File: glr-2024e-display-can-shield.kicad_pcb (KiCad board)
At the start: 2 copper layers, 10 parts, among them CN12 Conn_02x08_Odd_Even, CN6 Conn_01x08, CN8 Conn_01x06, IC1 L9615D013TR, J1 Screw_Terminal_01x12

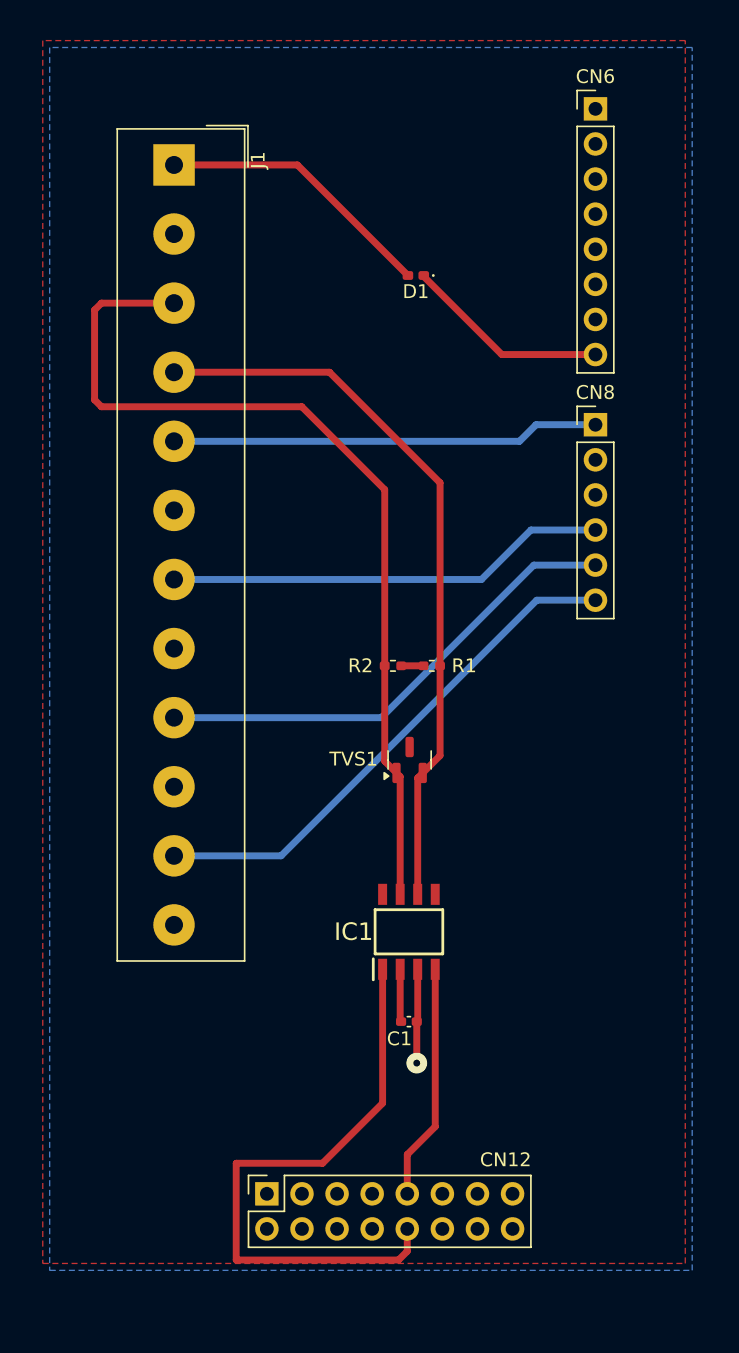
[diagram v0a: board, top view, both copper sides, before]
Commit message: make 4pin and 8pin screw terminal instead of 12pin
use exact footprint and 3d model

Co-Authored-By: wallalex0 <97884125+wallalex0@users.noreply.github.com>
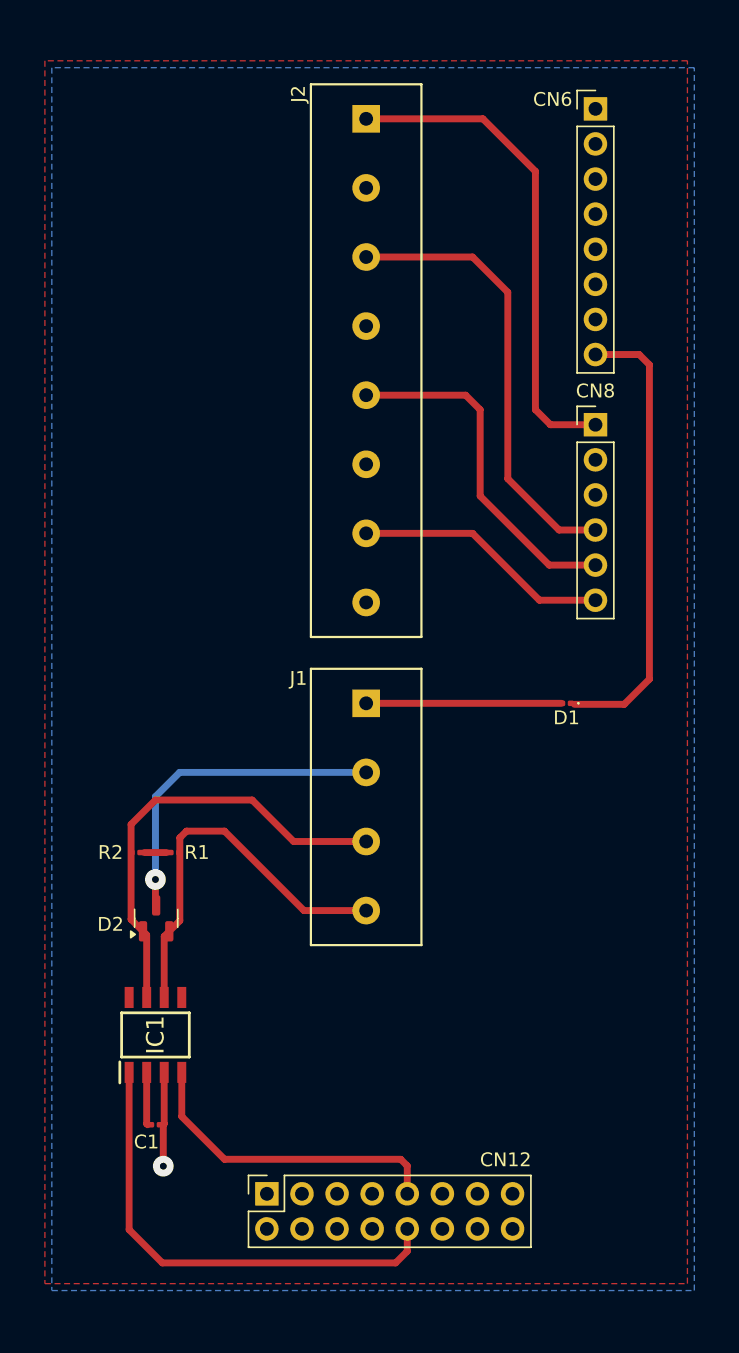
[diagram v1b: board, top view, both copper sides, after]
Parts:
- added J2: Screw_Terminal_01x08, GLR_KiCAD_Library:WECO-950-FB-08, F.Cu at (140.1, 47.7)
- C1: footprint Capacitor_SMD:C_0402_1005Metric_Pad0.74x0.62mm_HandSolder -> Capacitor_SMD:C_0201_0603Metric
- D1: footprint Diode_SMD:D_0402_1005Metric_Pad0.77x0.64mm_HandSolder -> Diode_SMD:D_0201_0603Metric
- J1: value Screw_Terminal_01x12 -> Screw_Terminal_01x04; footprint TerminalBlock_Altech:Altech_AK100_1x12_P5.00mm -> GLR_KiCAD_Library:WECO-950-FB-04
- R1, R2: footprint Resistor_SMD:R_0402_1005Metric_Pad0.72x0.64mm_HandSolder -> Resistor_SMD:R_0201_0603Metric
- moved J1 58.3 mm to (140.9, 110.0), turned to 180 degrees
- moved D1 32.8 mm to (155.0, 92.5)
- moved R1 23.0 mm to (126.7, 103.3)
- moved R2 23.0 mm to (123.8, 103.3)
- moved D2 21.6 mm to (125.3, 108.1)
- moved C1 19.8 mm to (125.2, 123.0)
- moved IC1 19.8 mm to (125.2, 116.5)
- renumbered TVS1 to D2
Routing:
- net /CAN H: track 65.9 -> 32.0 mm
- net /CAN L: track 53.0 -> 28.1 mm
- net GND: track 3.82 -> 27.7 mm, vias 0 -> 1
- net /button4: track 38.2 -> 18.6 mm
- net +6V to +9V: track 14.8 -> 33.1 mm
- net /button3: track 35.1 -> 25.4 mm
- net /Tx: track 43.3 -> 34.5 mm
- net Net-(D1-A): track 20.2 -> 14.1 mm
- net /Rx: track 17.1 -> 23.0 mm
- net /button1: track 31.0 -> 35.9 mm
- net /button2: track 32.0 -> 32.7 mm

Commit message: add voltage regulator 12V -> 8V
improve alignment of connectors
add board outline
add descriptions

Co-Authored-By: wallalex0 <97884125+wallalex0@users.noreply.github.com>
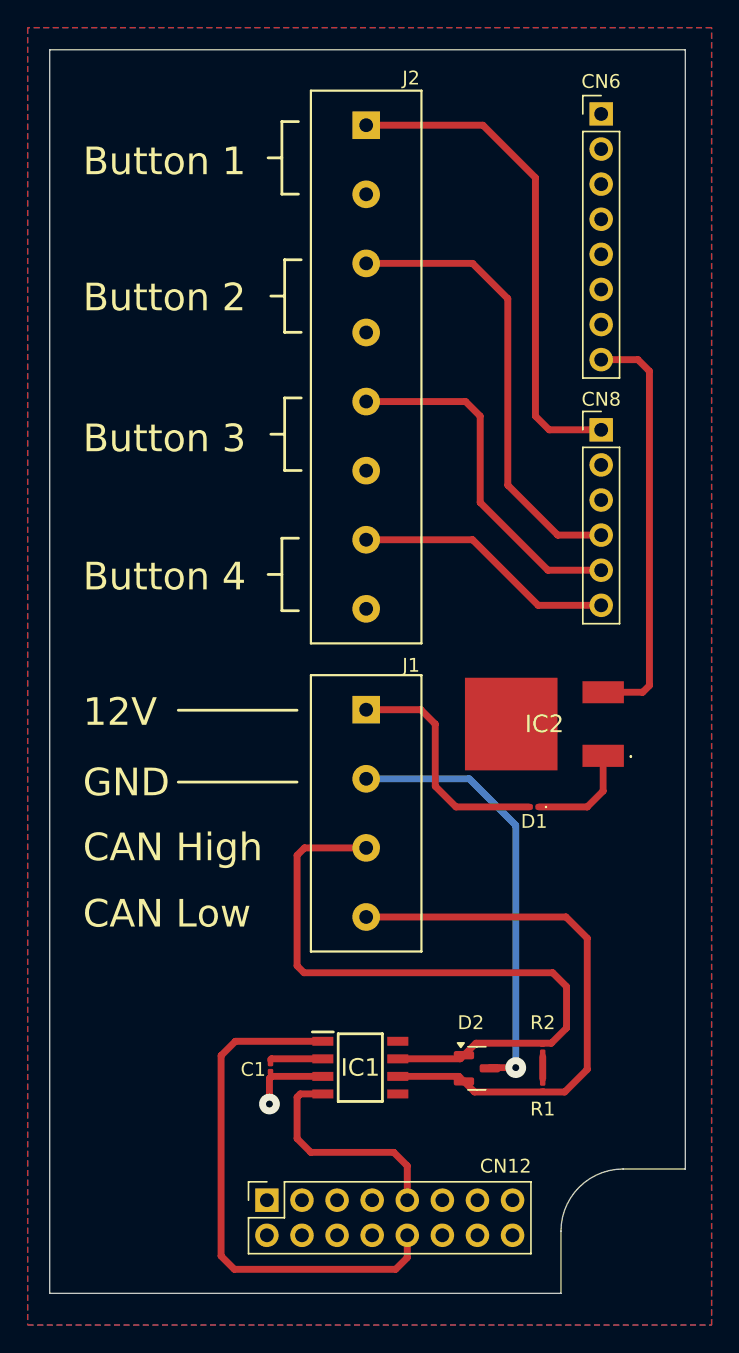
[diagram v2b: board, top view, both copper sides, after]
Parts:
- added IC2: LF80CDT-TR, SamacSys_Parts:LF80CDTTR, F.Cu at (153.1, 94.0)
- moved R2 32.7 mm to (153.3, 117.5), turned to 90 degrees
- moved R1 31.6 mm to (153.3, 120.3), turned to 90 degrees
- moved D2 25.6 mm to (148.5, 118.9), turned to 0 degrees
- moved IC1 15.0 mm to (140.1, 118.9), turned to 0 degrees
- moved C1 9.30 mm to (133.6, 118.9), turned to -90 degrees
- moved D1 7.86 mm to (152.7, 100.0)
- moved CN8 0.55 mm to (157.5, 72.7)
- moved CN6 0.55 mm to (157.5, 49.8)
- moved CN12 0.46 mm to (133.3, 128.5)
- moved J1 0.46 mm to (140.9, 110.5)
- moved J2 0.46 mm to (140.1, 48.2)
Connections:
- CN6 pad 8: +6V to +9V -> +8V
- D1 pad 1: +6V to +9V -> /+12V
- D1 pad 2: Net-(D1-A) -> /+12V
- J1 pad 1: Net-(D1-A) -> /+12V
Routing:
- net +6V to +9V: track 33.1 -> 0.00 mm
- net +8V: track 0.00 -> 30.1 mm
- net /+12V: track 0.00 -> 25.0 mm
- net /CAN H: track 32.0 -> 49.5 mm
- net Net-(D1-A): track 14.1 -> 0.00 mm
- net /CAN L: track 28.1 -> 41.0 mm
- net GND: track 27.7 -> 35.5 mm
- net /Rx: track 23.0 -> 16.2 mm
- net /Tx: track 34.5 -> 38.1 mm
- net +5V: track 6.82 -> 5.78 mm
- net /button4: track 18.6 -> 19.1 mm
- net /button1: track 35.9 -> 36.4 mm
- net /button3: track 25.4 -> 25.9 mm
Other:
- board outline added: 46 x 90 mm
- board text added: "12V"
- board text added: "Button 1"
- board text added: "Button 2"
- board text added: "Button 3"
- board text added: "Button 4"
- board text added: "CAN High"
- board text added: "CAN Low"
- board text added: "GND"

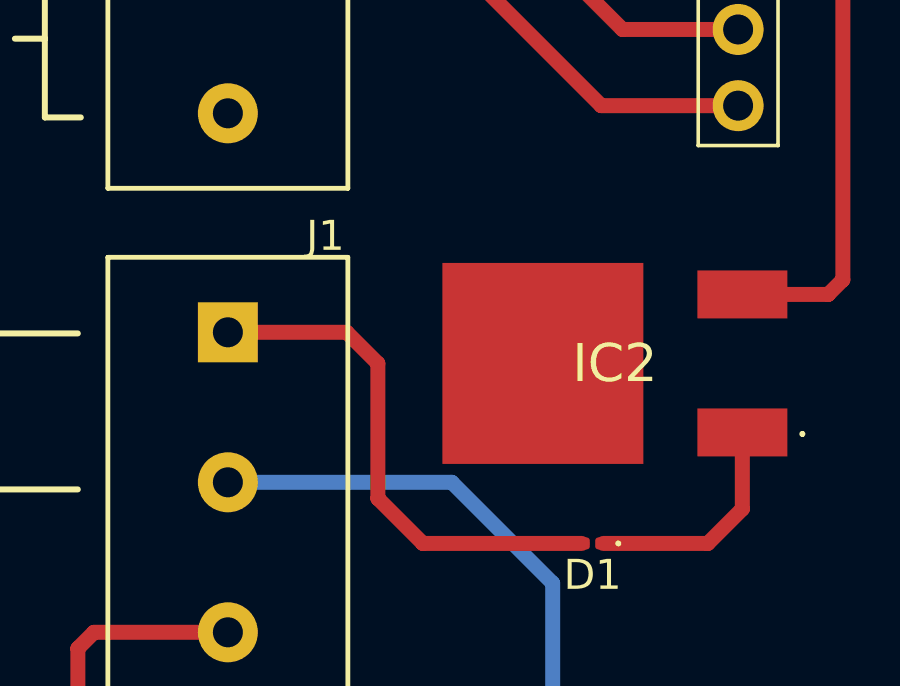
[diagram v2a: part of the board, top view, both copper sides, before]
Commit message: add board infos on pcb
add two no GND zones

Co-Authored-By: wallalex0 <97884125+wallalex0@users.noreply.github.com>
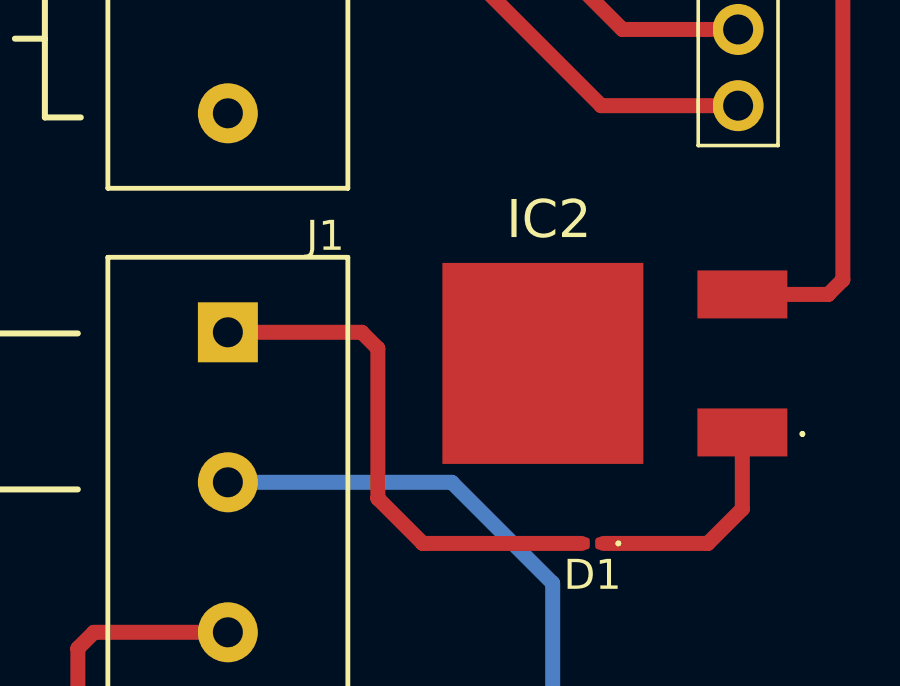
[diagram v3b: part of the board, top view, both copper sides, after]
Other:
- board text added: "${COMPANY} ${TITLE} ${PROJECTNAME} ${REVISION} ${ISSUE_DATE}"
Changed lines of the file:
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@@
 	(title_block
 		(title "CAN-Shield for STM32F469I-DISCO")
-		(date "2025-02-15")
+		(date "2025-02-18")
 		(rev "v3")
 		(company "Green Lion Racing")
@@
 		(tags "Integrated Circuit")
 		(property "Reference" "IC2"
-			(at 0.35 0 0)
+			(at -1.85 -4.8 0)
 			(layer "F.SilkS")
 			(effects
@@
 		(descr "WECO-950-FB-08 StepUp generated footprint")
 		(property "Reference" "J2"
-			(at -0.912 -3.688 360)
+			(at -0.912 -3.688 0)
 			(layer "F.SilkS")
 			(effects
@@
 		(tags "diode")
 		(property "Reference" "D1"
-			(at 0 -1.05 360)
+			(at 0 -1.05 0)
 			(layer "F.SilkS")
 			(effects
@@
 		)
 		(property "Value" "D_Filled"
-			(at 0 1.05 360)
+			(at 0 1.05 0)
 			(layer "F.Fab")
 			(hide yes)
@@
 		)
 		(fp_text user "${REFERENCE}"
-			(at 0 -0.68 360)
+			(at 0 -0.68 0)
 			(layer "F.Fab")
 			(effects
@@
 		(layer "Edge.Cuts")
 	)
+	(gr_text "${COMPANY}\n${TITLE}\n${PROJECTNAME} ${REVISION}\n${ISSUE_DATE}"
+		(at 132.5 47.6 90)
+		(layer "B.SilkS")
+		(effects
+			(font
+				(size 2 2)
+				(thickness 0.2)
+			)
+			(justify left bottom mirror)
+		)
+	)
 	(gr_text "Button 4"
 		(at 120 84.5 0)
@@
 	)
 	(segment
-		(start 157.65 98.85)
-		(end 156.5 100)
+		(start 145.5 98.5)
+		(end 147 100)
 		(width 0.5)
 		(layer "F.Cu")
@@
 	)
 	(segment
-		(start 140.5 92.962)
-		(end 144.462 92.962)
+		(start 157.65 98.85)
+		(end 156.5 100)
 		(width 0.5)
 		(layer "F.Cu")
@@
 	)
 	(segment
-		(start 147 100)
-		(end 152.295 100)
+		(start 157.65 96.3)
+		(end 157.65 98.85)
 		(width 0.5)
 		(layer "F.Cu")
@@
 	)
 	(segment
-		(start 145.5 98.5)
-		(end 147 100)
+		(start 140.5 92.962)
+		(end 144.962 92.962)
 		(width 0.5)
 		(layer "F.Cu")
@@
 	)
 	(segment
-		(start 144.462 92.962)
-		(end 145.5 94)
+		(start 144.962 92.962)
+		(end 145.5 93.5)
 		(width 0.5)
 		(layer "F.Cu")
@@
 	)
 	(segment
-		(start 157.65 96.3)
-		(end 157.65 98.85)
+		(start 147 100)
+		(end 152.295 100)
 		(width 0.5)
 		(layer "F.Cu")
@@
 	)
 	(segment
-		(start 145.5 94)
+		(start 145.5 93.5)
 		(end 145.5 98.5)
 		(width 0.5)
@@
 	)
 	(zone
+		(net 0)
+		(net_name "")
+		(layer "F.Cu")
+		(name "noGroundZone")
+		(hatch edge 0.5)
+		(connect_pads
+			(clearance 0)
+		)
+		(min_thickness 0.25)
+		(filled_areas_thickness no)
+		(keepout
+			(tracks allowed)
+			(vias allowed)
+			(pads allowed)
+			(copperpour not_allowed)
+			(footprints allowed)
+		)
+		(fill
+			(thermal_gap 0.5)
+			(thermal_bridge_width 0.5)
+		)
+		(polygon
+			(pts
+				(xy 147.6 117.4) (xy 152.8 117.4) (xy 152.8 120.4) (xy 147.6 120.4)
+			)
+		)
+	)
+	(zone
+		(net 0)
+		(net_name "")
+		(layer "F.Cu")
+		(name "noGroundZone")
+		(hatch edge 0.5)
+		(connect_pads
+			(clearance 0)
+		)
+		(min_thickness 0.25)
+		(filled_areas_thickness no)
+		(keepout
+			(tracks allowed)
+			(vias allowed)
+			(pads allowed)
+			(copperpour not_allowed)
+			(footprints allowed)
+		)
+		(fill
+			(thermal_gap 0.5)
+			(thermal_bridge_width 0.5)
+		)
+		(polygon
+			(pts
+				(xy 133 117.4) (xy 136.4 117.4) (xy 136.4 119) (xy 133 119)
+			)
+		)
+	)
+	(zone

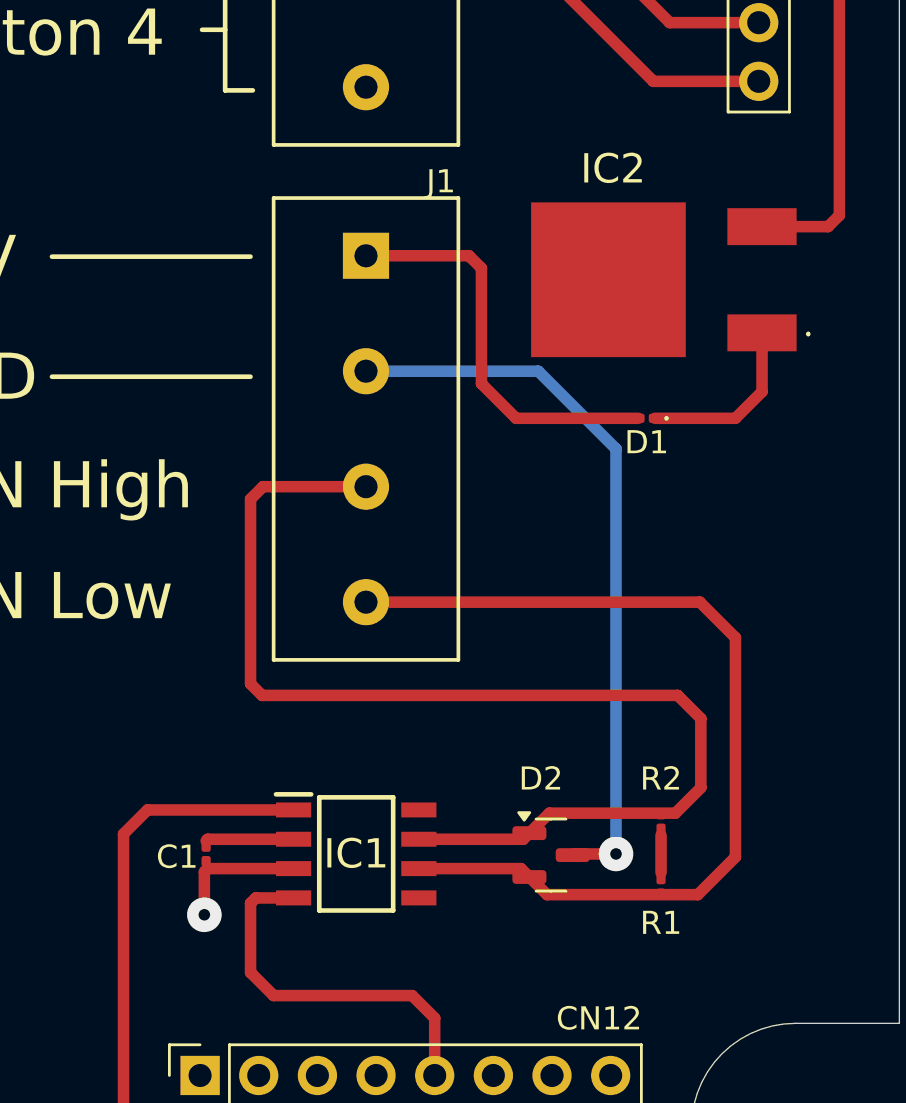
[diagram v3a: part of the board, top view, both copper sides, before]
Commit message: explicitly define which parts to use
Co-Authored-By: wallalex0 <97884125+wallalex0@users.noreply.github.com>
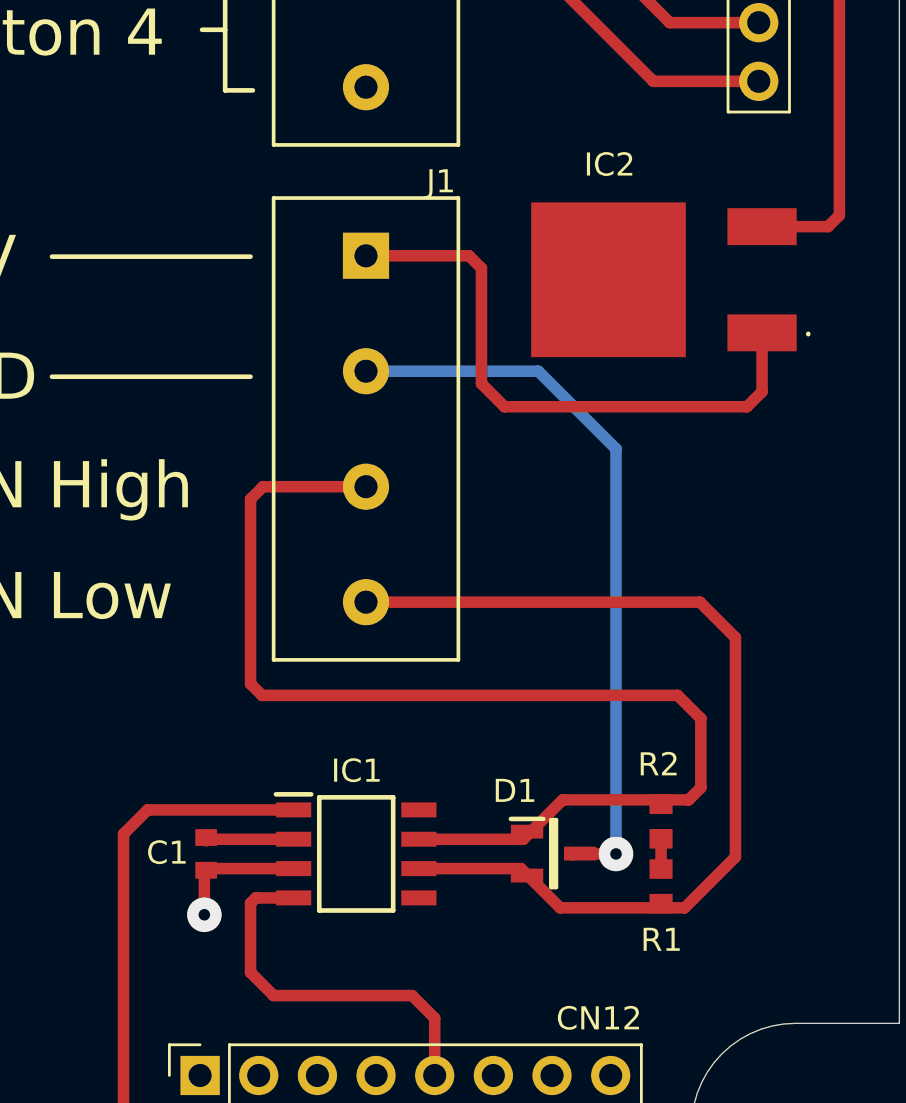
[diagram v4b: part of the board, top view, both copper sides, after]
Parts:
- removed D2: D_TVS_Dual_AAC, Package_TO_SOT_SMD:SOT-23
- C1: value 0.1μF 16V -> 0.1μF 50V; footprint Capacitor_SMD:C_0201_0603Metric -> SamacSys_Parts:CAPC1608X90N
- D1: value D_Filled -> ESDCAN01-2BLY; footprint Diode_SMD:D_0201_0603Metric -> SamacSys_Parts:SOT95P255X125-3N
- R1, R2: footprint Resistor_SMD:R_0201_0603Metric -> SamacSys_Parts:RESC1608X50N
- moved D1 19.3 mm to (148.6, 118.8), turned to 0 degrees
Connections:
- C1 pad 1: GND -> +5V
- C1 pad 2: +5V -> GND
- D1 pad 1: /+12V -> /CAN H
- D1 pad 2: /+12V -> /CAN L
